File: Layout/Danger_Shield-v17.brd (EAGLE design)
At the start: 80 x 105.4 mm, 35 parts, among them U1 ARDUINO_SHIELD, U2 74LS595N, U4 TMP36

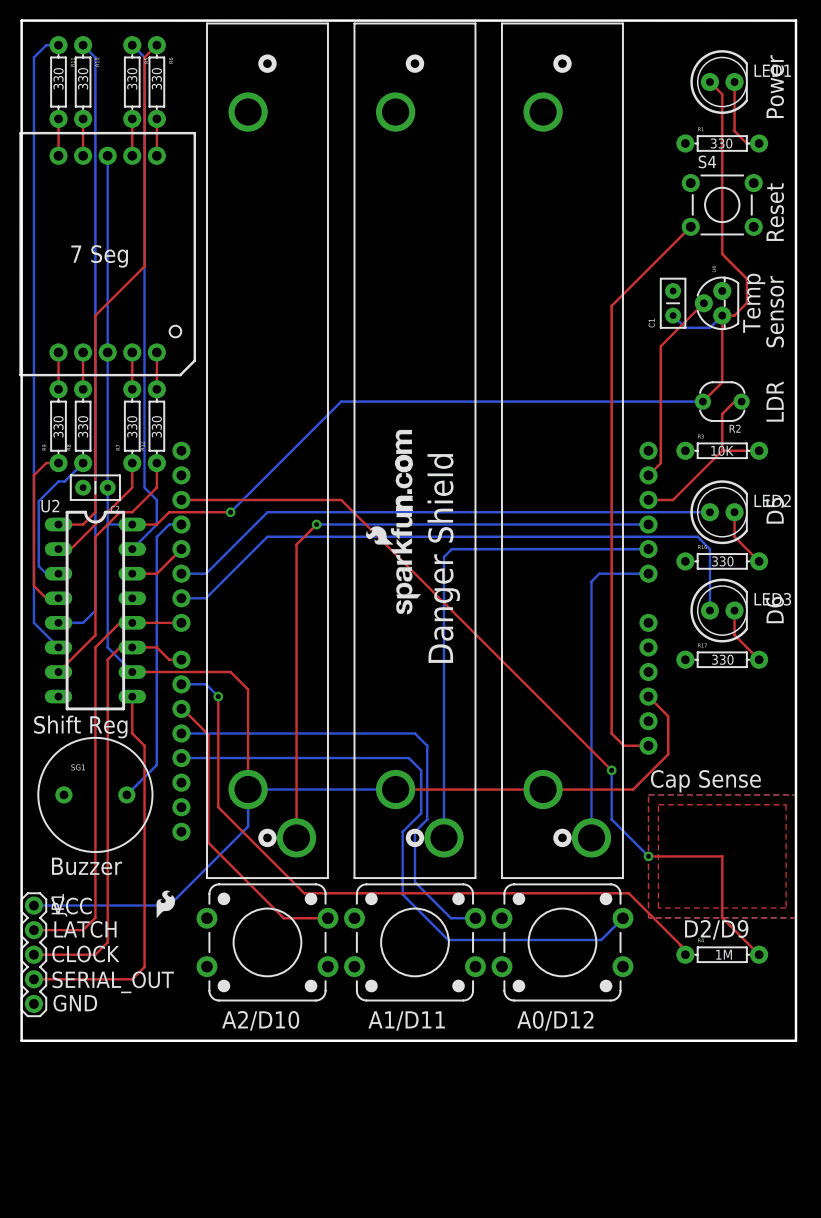
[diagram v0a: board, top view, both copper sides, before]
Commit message: Added CC license to schematic and PCB.
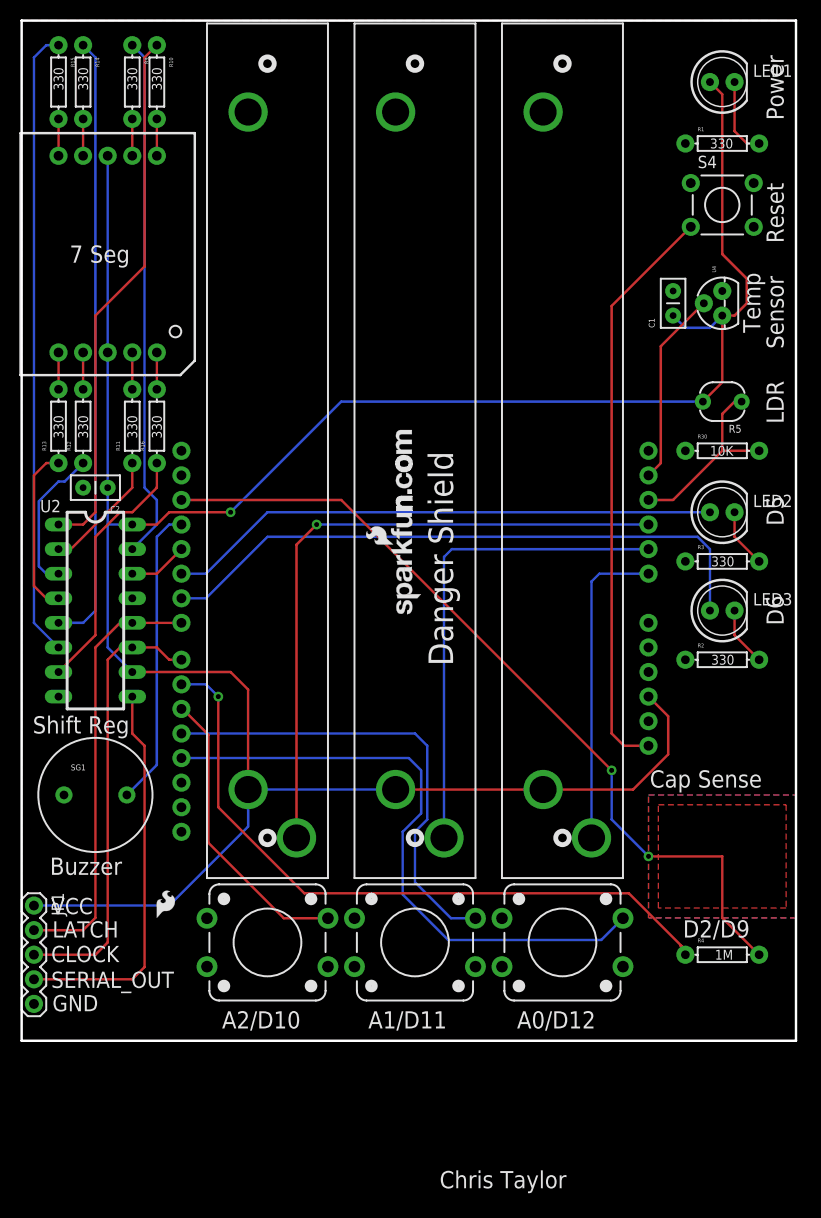
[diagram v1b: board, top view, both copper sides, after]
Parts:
- removed R17, R7: 330, SparkFun:AXIAL-0.3
- removed R18, R20: SLIDER, SparkFun:SLIDER
- added R13, R14, R15: 330, SparkFun:AXIAL-0.3
- added R30: 10K, SparkFun:AXIAL-0.3
- added U$1: CREATIVE_COMMONS, SparkFun-Aesthetics:CREATIVE_COMMONS
- R2: value PHOTOCELLPTH -> 330; device SparkFun:PHOTOCELL -> SparkFun:AXIAL-0.3
- R3: value 10K -> 330
- R5: value 330 -> CdS; device SparkFun:AXIAL-0.3 -> SparkFun:PHOTOCELL
- R6: value 330 -> Slider3; device SparkFun:AXIAL-0.3 -> SparkFun:SLIDER
- R7\: value SLIDER -> Slider2
- R8: value 330 -> Slider1; device SparkFun:AXIAL-0.3 -> SparkFun:SLIDER
- moved R5 69.3 mm to (72.4, 66.0), turned to 180 degrees
- moved R16 60.1 mm to (14.0, 63.5), turned to 90 degrees
- moved R8 49.6 mm to (55.9, 61.0)
- moved R6 39.8 mm to (25.4, 61.0), turned to 90 degrees
- moved R11 36.4 mm to (11.4, 63.5), turned to 90 degrees
- moved R9 36.4 mm to (11.4, 99.1), turned to 270 degrees
- moved R2 26.7 mm to (72.4, 39.4), turned to 0 degrees
- moved R3 11.4 mm to (72.4, 49.5)
- moved R10 7.62 mm to (14.0, 99.1)
- moved R12 7.62 mm to (6.35, 63.5)
- renumbered R19 to R7\
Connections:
- net A0: now also R8.2A; no longer R20.2A
- net A2: now also R6.2A; no longer R18.2A
- net A3: now also R30.P$2, R5.1; no longer R2.1, R3.P$2
- net GND: now also R2.P$1, R30.P$1, R6.3, R8.3; no longer R16.P$1, R17.P$1, R18.3, R20.3
- net N$10: now also R16.P$1; no longer R12.P$1
- net N$11: now also R9.P$2; no longer R5.P$2
- net N$12: now also R10.P$2; no longer R6.P$2
- net N$13: now also R11.P$2; no longer R7.P$2
- net N$14: now also R12.P$2; no longer R8.P$2
- net N$15: now also R13.P$2; no longer R9.P$2
- net N$16: now also R14.P$2; no longer R10.P$2
- net N$17: now also R15.P$2; no longer R11.P$2
- net N$18: now also R16.P$2; no longer R12.P$2
- net N$19: now also R2.P$2; no longer R17.P$2
- net N$2: now also R9.P$1; no longer R5.P$1
- net N$20: now also R3.P$2; no longer R16.P$2
- net N$4: now also R10.P$1; no longer R6.P$1
- net N$5: now also R11.P$1; no longer R7.P$1
- net N$6: now also R12.P$1; no longer R8.P$1
- net N$7: now also R13.P$1; no longer R9.P$1
- net N$8: now also R14.P$1; no longer R10.P$1
- net N$9: now also R15.P$1; no longer R11.P$1
- net VCC: now also R5.2, R6.1, R8.1; no longer R18.1, R2.2, R20.1
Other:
- board text added: "Chris Taylor"

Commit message: Added version # 1.7 to PCB.
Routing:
- net A1: track 50.5 -> 47.5 mm
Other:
- board text added: "v1.7"
- board text removed: "MakerBot.com"

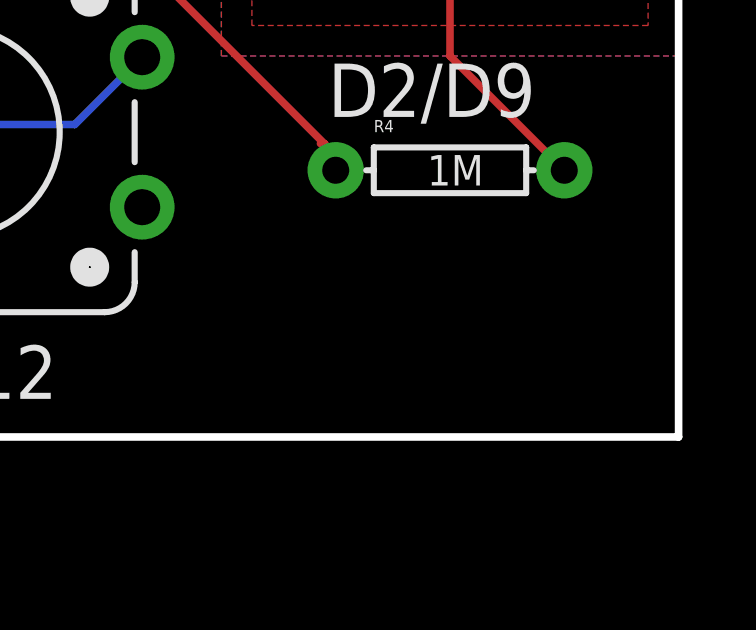
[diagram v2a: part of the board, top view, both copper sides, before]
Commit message: Update to gitignore. Added OSHW logo. Fixed overlapping resistors.
Cleaned up the example code slightly as well. Trying to fit into
SparkFun coding standards.
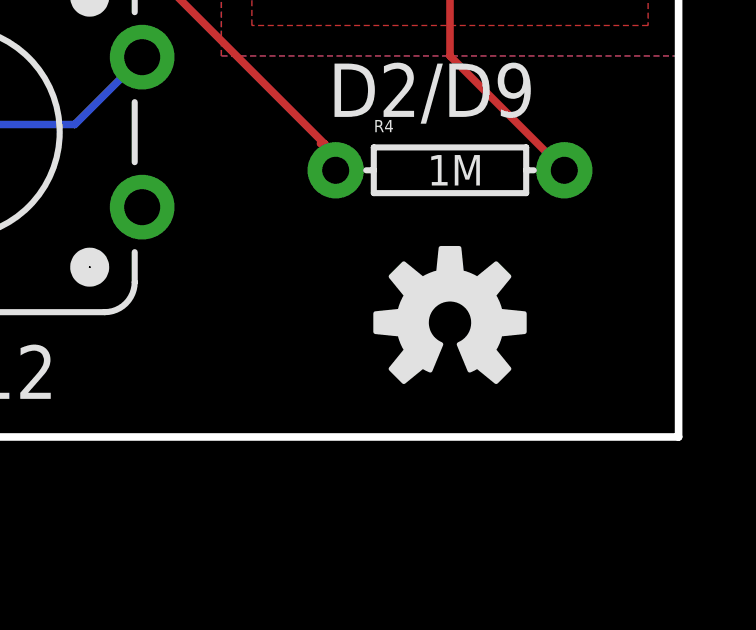
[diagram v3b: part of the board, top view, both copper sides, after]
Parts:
- added U$2: OSHW-LOGOM, SparkFun-Aesthetics:OSHW-LOGO-M
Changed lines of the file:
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@@
 <?xml version="1.0" encoding="utf-8"?>
 <!DOCTYPE eagle SYSTEM "eagle.dtd">
-<eagle version="6.2">
+<eagle version="6.3">
 <drawing>
 <settings>
@@
 <layer number="19" name="Unrouted" color="6" fill="1" visible="yes" active="yes"/>
 <layer number="20" name="Dimension" color="15" fill="1" visible="yes" active="yes"/>
-<layer number="21" name="tPlace" color="24" fill="1" visible="yes" active="yes"/>
+<layer number="21" name="tPlace" color="16" fill="1" visible="yes" active="yes"/>
 <layer number="22" name="bPlace" color="14" fill="1" visible="yes" active="yes"/>
 <layer number="23" name="tOrigins" color="15" fill="1" visible="yes" active="yes"/>
@@
 </class>
 </classes>
-<designrules>
+<designrules name="default">
 <description language="en">&lt;b&gt;EAGLE Design Rules&lt;/b&gt;
 &lt;p&gt;
@@
 <element name="C2" library="SparkFun-Passives" package="CAP-PTH-SMALL2" value="0.1uF" x="8.89" y="57.15" rot="R180"/>
 <element name="U$1" library="SparkFun-Aesthetics" package="CREATIVE_COMMONS" value="CREATIVE_COMMONS" x="11.43" y="-15.24"/>
+<element name="U$2" library="SparkFun-Aesthetics" package="OSHW-LOGO-M" value="OSHW-LOGOM" x="72.39" y="3.81"/>
 </elements>
 <signals>

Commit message: Adding dimensional and BOM.
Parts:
- renumbered R7\ to R7, U$6 to U6
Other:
- board text added: "0"
- board text added: "3150"
- board text added: "4150"
- board text added: "All Dimensions in mil"
- board text added: "Spark Fun Electronics"
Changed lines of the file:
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@@
 <grid distance="0.05" unitdist="inch" unit="inch" style="lines" multiple="1" display="yes" altdistance="0.005" altunitdist="inch" altunit="inch"/>
 <layers>
-<layer number="1" name="Top" color="4" fill="1" visible="yes" active="yes"/>
+<layer number="1" name="Top" color="4" fill="1" visible="no" active="yes"/>
 <layer number="2" name="Route2" color="1" fill="3" visible="no" active="no"/>
 <layer number="3" name="Route3" color="4" fill="3" visible="no" active="no"/>
@@
 <layer number="14" name="Route14" color="1" fill="6" visible="no" active="no"/>
 <layer number="15" name="Route15" color="4" fill="6" visible="no" active="no"/>
-<layer number="16" name="Bottom" color="1" fill="1" visible="yes" active="yes"/>
+<layer number="16" name="Bottom" color="1" fill="1" visible="no" active="yes"/>
 <layer number="17" name="Pads" color="2" fill="1" visible="yes" active="yes"/>
 <layer number="18" name="Vias" color="2" fill="1" visible="yes" active="yes"/>
 <layer number="19" name="Unrouted" color="6" fill="1" visible="yes" active="yes"/>
 <layer number="20" name="Dimension" color="15" fill="1" visible="yes" active="yes"/>
-<layer number="21" name="tPlace" color="16" fill="1" visible="yes" active="yes"/>
+<layer number="21" name="tPlace" color="16" fill="1" visible="no" active="yes"/>
 <layer number="22" name="bPlace" color="14" fill="1" visible="yes" active="yes"/>
 <layer number="23" name="tOrigins" color="15" fill="1" visible="yes" active="yes"/>
@@
 <layer number="45" name="Holes" color="7" fill="1" visible="yes" active="yes"/>
 <layer number="46" name="Milling" color="3" fill="1" visible="no" active="yes"/>
-<layer number="47" name="Measures" color="7" fill="1" visible="no" active="yes"/>
+<layer number="47" name="Measures" color="7" fill="1" visible="yes" active="yes"/>
 <layer number="48" name="Document" color="7" fill="1" visible="no" active="yes"/>
 <layer number="49" name="Reference" color="7" fill="1" visible="no" active="yes"/>
 <layer number="50" name="dxf" color="7" fill="1" visible="no" active="yes"/>
-<layer number="51" name="tDocu" color="6" fill="1" visible="yes" active="yes"/>
+<layer number="51" name="tDocu" color="6" fill="1" visible="no" active="yes"/>
 <layer number="52" name="bDocu" color="7" fill="1" visible="no" active="yes"/>
 <layer number="53" name="tGND_GNDA" color="7" fill="9" visible="no" active="no"/>
@@
 <wire x1="72.39" y1="109.22" x2="72.39" y2="-7.62" width="0.254" layer="51"/>
 <wire x1="78.74" y1="109.22" x2="78.74" y2="-7.62" width="0.254" layer="51"/>
-<wire x1="-7.62" y1="53.34" x2="90.17" y2="53.34" width="0.254" layer="51"/>
 <wire x1="-10.16" y1="25.4" x2="83.82" y2="25.4" width="0.254" layer="51"/>
 <text x="20.701" y="1.27" size="1.778" layer="21" ratio="15">A2/D10</text>
@@
 <text x="43.18" y="-15.24" size="1.778" layer="21">Chris Taylor</text>
 <text x="43.18" y="48.26" size="1.778" layer="16" ratio="15" rot="MR0">v1.7</text>
+<text x="80.01" y="-6.35761875" size="1.016" layer="47" font="vector" rot="R90">3150</text>
+<wire x1="80.01" y1="-0.635" x2="80.01" y2="-11.4935" width="0.0635" layer="47"/>
+<wire x1="80.01" y1="-11.4935" x2="80.01" y2="-14.478" width="0.0635" layer="47"/>
+<wire x1="0" y1="-0.635" x2="0" y2="-11.4935" width="0.1016" layer="47"/>
+<text x="0" y="-6.35761875" size="1.016" layer="47" font="vector" rot="R90">0</text>
+<text x="0" y="-6.35761875" size="1.016" layer="47" font="vector" rot="R90">0</text>
+<wire x1="0" y1="-11.4935" x2="0" y2="-14.478" width="0.1016" layer="47"/>
+<wire x1="0" y1="-11.4935" x2="80.01" y2="-11.4935" width="0.0635" layer="47"/>
+<text x="-6.35761875" y="105.41" size="1.016" layer="47" font="vector">4150</text>
+<wire x1="-0.635" y1="105.41" x2="-11.4935" y2="105.41" width="0.0635" layer="47"/>
+<wire x1="-11.4935" y1="105.41" x2="-14.478" y2="105.41" width="0.0635" layer="47"/>
+<circle x="-11.4935" y="0" radius="0.0635" width="0" layer="47"/>
+<wire x1="-0.635" y1="0" x2="-11.4935" y2="0" width="0.1016" layer="47"/>
+<text x="-6.35761875" y="0" size="1.016" layer="47" font="vector">0</text>
+<text x="-6.35761875" y="0" size="1.016" layer="47" font="vector">0</text>
+<wire x1="-11.4935" y1="0" x2="-14.478" y2="0" width="0.1016" layer="47"/>
+<wire x1="-11.4935" y1="0" x2="-11.4935" y2="105.41" width="0.0635" layer="47"/>
+<text x="-27.94" y="-5.08" size="1.016" layer="47" font="vector">All Dimensions in mil</text>
+<text x="-27.94" y="-6.4008" size="1.016" layer="47" font="vector">Spark Fun Electronics</text>
 </plain>
 <attributes>
@@
 <elements>
 <element name="R8" library="SparkFun" package="SLIDER" value="Slider1" x="55.88" y="60.96" rot="R90"/>
-<element name="R7\" library="SparkFun" package="SLIDER" value="Slider2" x="40.64" y="60.96" rot="R90"/>
+<element name="R7" library="SparkFun" package="SLIDER" value="Slider2" x="40.64" y="60.96" rot="R90"/>
 <element name="R6" library="SparkFun" package="SLIDER" value="Slider3" x="25.4" y="60.96" rot="R90"/>
 <element name="R1" library="SparkFun" package="AXIAL-0.3" value="330" x="72.39" y="92.71" smashed="yes">
@@
 <element name="JP3" library="SparkFun" package="SFE-NEW-WEBLOGO" value="LOGO-SFENEW" x="50.8" y="62.23" rot="MR0"/>
 <element name="JP5" library="SparkFun" package="SFE-LOGO-FLAME" value="LOGO-SFESK" x="13.97" y="12.7"/>
-<element name="U$6" library="SparkFun" package="7-SEGMENT-1&quot;PTH" value="7-SEGMENT-DISPLAY-1&quot;-RED" x="8.89" y="81.28"/>
+<element name="U6" library="SparkFun" package="7-SEGMENT-1&quot;PTH" value="7-SEGMENT-DISPLAY-1&quot;-RED" x="8.89" y="81.28"/>
 <element name="S2" library="SparkFun" package="TACTILE-PTH-12MM" value="Button2" x="40.64" y="10.16"/>
 <element name="S1" library="SparkFun" package="TACTILE-PTH-12MM" value="Button1" x="25.4" y="10.16"/>
@@
 <signal name="VCC">
 <contactref element="R6" pad="1"/>
-<contactref element="R7\" pad="1"/>
+<contactref element="R7" pad="1"/>
 <contactref element="R8" pad="1"/>
 <contactref element="LED1" pad="A"/>
@@
 <contactref element="JP1" pad="1"/>
 <contactref element="U1" pad="5V"/>
-<contactref element="U$6" pad="3"/>
-<contactref element="U$6" pad="8"/>
+<contactref element="U6" pad="3"/>
+<contactref element="U6" pad="8"/>
 <wire x1="23.4" y1="25.96" x2="38.64" y2="25.96" width="0.254" layer="16"/>
 <wire x1="38.64" y1="25.96" x2="53.88" y2="25.96" width="0.254" layer="1"/>
@@
 <signal name="GND" airwireshidden="yes">
 <contactref element="R6" pad="3"/>
-<contactref element="R7\" pad="3"/>
+<contactref element="R7" pad="3"/>
 <contactref element="R8" pad="3"/>
 <contactref element="R1" pad="P$1"/>
@@
 </signal>
 <signal name="A1">
-<contactref element="R7\" pad="2A"/>
+<contactref element="R7" pad="2A"/>
 <contactref element="U1" pad="A1"/>
 <wire x1="43.64" y1="20.96" x2="43.64" y2="44.91" width="0.254" layer="16"/>
@@
 <signal name="N$11">
 <contactref element="R9" pad="P$2"/>
-<contactref element="U$6" pad="7"/>
+<contactref element="U6" pad="7"/>
 <wire x1="11.43" y1="91.44" x2="11.43" y2="95.25" width="0.254" layer="1"/>
 </signal>
 <signal name="N$12">
 <contactref element="R10" pad="P$2"/>
-<contactref element="U$6" pad="6"/>
+<contactref element="U6" pad="6"/>
 <wire x1="13.97" y1="91.44" x2="13.97" y2="95.25" width="0.254" layer="1"/>
 </signal>
 <signal name="N$13">
 <contactref element="R11" pad="P$2"/>
-<contactref element="U$6" pad="4"/>
+<contactref element="U6" pad="4"/>
 <wire x1="11.43" y1="67.31" x2="11.43" y2="71.12" width="0.254" layer="1"/>
 </signal>
 <signal name="N$14">
 <contactref element="R12" pad="P$2"/>
-<contactref element="U$6" pad="2"/>
+<contactref element="U6" pad="2"/>
 <wire x1="6.35" y1="67.31" x2="6.35" y2="71.12" width="0.254" layer="1"/>
 </signal>
 <signal name="N$15">
 <contactref element="R13" pad="P$2"/>
-<contactref element="U$6" pad="1"/>
+<contactref element="U6" pad="1"/>
 <wire x1="3.81" y1="67.31" x2="3.81" y2="71.12" width="0.254" layer="1"/>
 </signal>
 <signal name="N$16">
 <contactref element="R14" pad="P$2"/>
-<contactref element="U$6" pad="9"/>
+<contactref element="U6" pad="9"/>
 <wire x1="6.35" y1="91.44" x2="6.35" y2="95.25" width="0.254" layer="1"/>
 </signal>
 <signal name="N$17">
 <contactref element="R15" pad="P$2"/>
-<contactref element="U$6" pad="10"/>
+<contactref element="U6" pad="10"/>
 <wire x1="3.81" y1="91.44" x2="3.81" y2="95.25" width="0.254" layer="1"/>
 </signal>
 <signal name="N$18">
 <contactref element="R16" pad="P$2"/>
-<contactref element="U$6" pad="5"/>
+<contactref element="U6" pad="5"/>
 <wire x1="13.97" y1="67.31" x2="13.97" y2="71.12" width="0.254" layer="1"/>
 </signal>
